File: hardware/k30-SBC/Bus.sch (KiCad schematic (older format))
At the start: 32 parts, among them J4 ADBUS-EXP, J5 ADBUS, J6 SIGBUS, J7 POWER, J8 POWER, J9 POWER, U12 74LS393, U2 74HC14, U3 74HC05, U4 74LS139, U5 4072, U6 74HC20, U7 74LS32, U8 74LS08

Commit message: Almost completed k30-SBC board design
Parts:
- removed C21: 0.1uF, Capacitor_THT:C_Disc_D3.0mm_W2.0mm_P2.50mm, symbol Device:C_Small
- C8: footprint Capacitor_THT:CP_Radial_D10.0mm_P5.00mm -> Capacitor_THT:CP_Radial_D8.0mm_P5.00mm
- J4: footprint Connector_PinHeader_2.54mm:PinHeader_2x20_P2.54mm_Vertical -> Connector_PinHeader_2.54mm:PinHeader_2x15_P2.54mm_Vertical; symbol Connector_Generic:Conn_02x20_Odd_Even -> Connector_Generic:Conn_02x15_Odd_Even
- U12: value 74LS393 -> 74HC393
- U4: value 74LS139 -> 74HC139
- U7: value 74LS32 -> 74HC32
- U8: value 74LS08 -> 74HC08
- renumbered C9 to C10, C12 to C11, C11 to C12, C14 to C13, C13 to C14, C16 to C15, C15 to C16, C18 to C17, C17 to C18, C20 to C19, C19 to C20, C5 to C4, C4 to C5, C7 to C6, C6 to C7, C10 to C9
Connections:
- no-connect marks 13 -> 3
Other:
- moved on the sheet: C10, C12, C14, C16, C18, C20, C5, C7

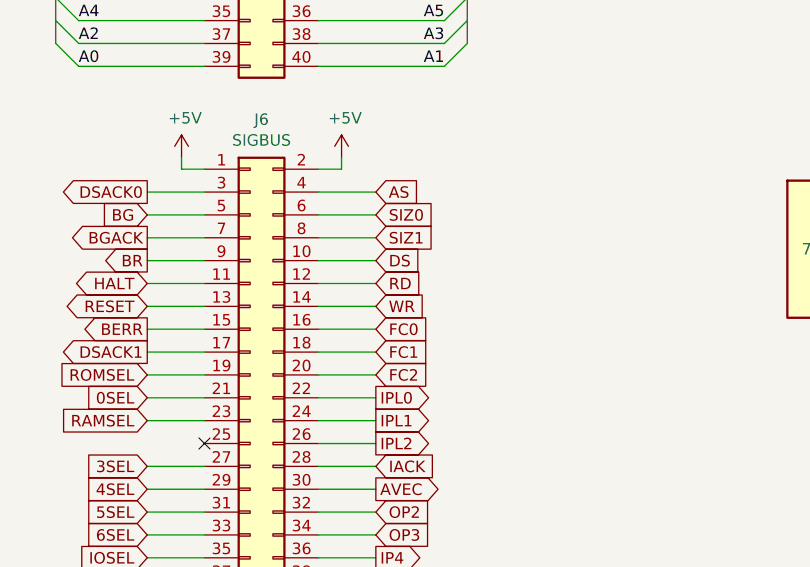
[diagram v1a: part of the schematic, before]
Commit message: Last minute changes: swapped WR/DS pins, added testpoint
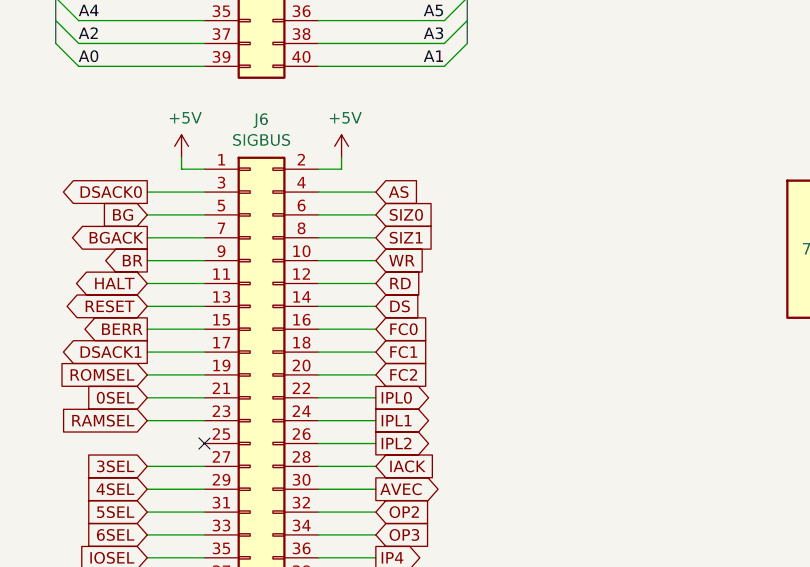
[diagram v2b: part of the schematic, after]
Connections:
- net DS: now also J6.14 (Pin_14); no longer J6.10 (Pin_10)
- net WR: now also J6.10 (Pin_10); no longer J6.14 (Pin_14)
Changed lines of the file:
@@
 Text GLabel 5100 5500 2    50   Input ~ 0
 IACK
-Text GLabel 5100 4600 2    50   Input ~ 0
+Text GLabel 5100 4800 2    50   Input ~ 0
 DS
 Wire Wire Line
-	5100 4600 4850 4600
+	5100 4800 4850 4800
 Text GLabel 5100 4700 2    50   Input ~ 0
 RD
-Text GLabel 5100 4800 2    50   Input ~ 0
+Text GLabel 5100 4600 2    50   Input ~ 0
 WR
 Wire Wire Line
 	4850 4700 5100 4700
 Wire Wire Line
-	5100 4800 4850 4800
+	5100 4600 4850 4600
 Wire Wire Line
 	4100 6000 4350 6000
